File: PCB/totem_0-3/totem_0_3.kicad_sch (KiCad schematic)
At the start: 88 parts, among them J1 MJ-4PP-9, J2 MJ-4PP-9, U1 xiao-ble, U2 xiao-ble

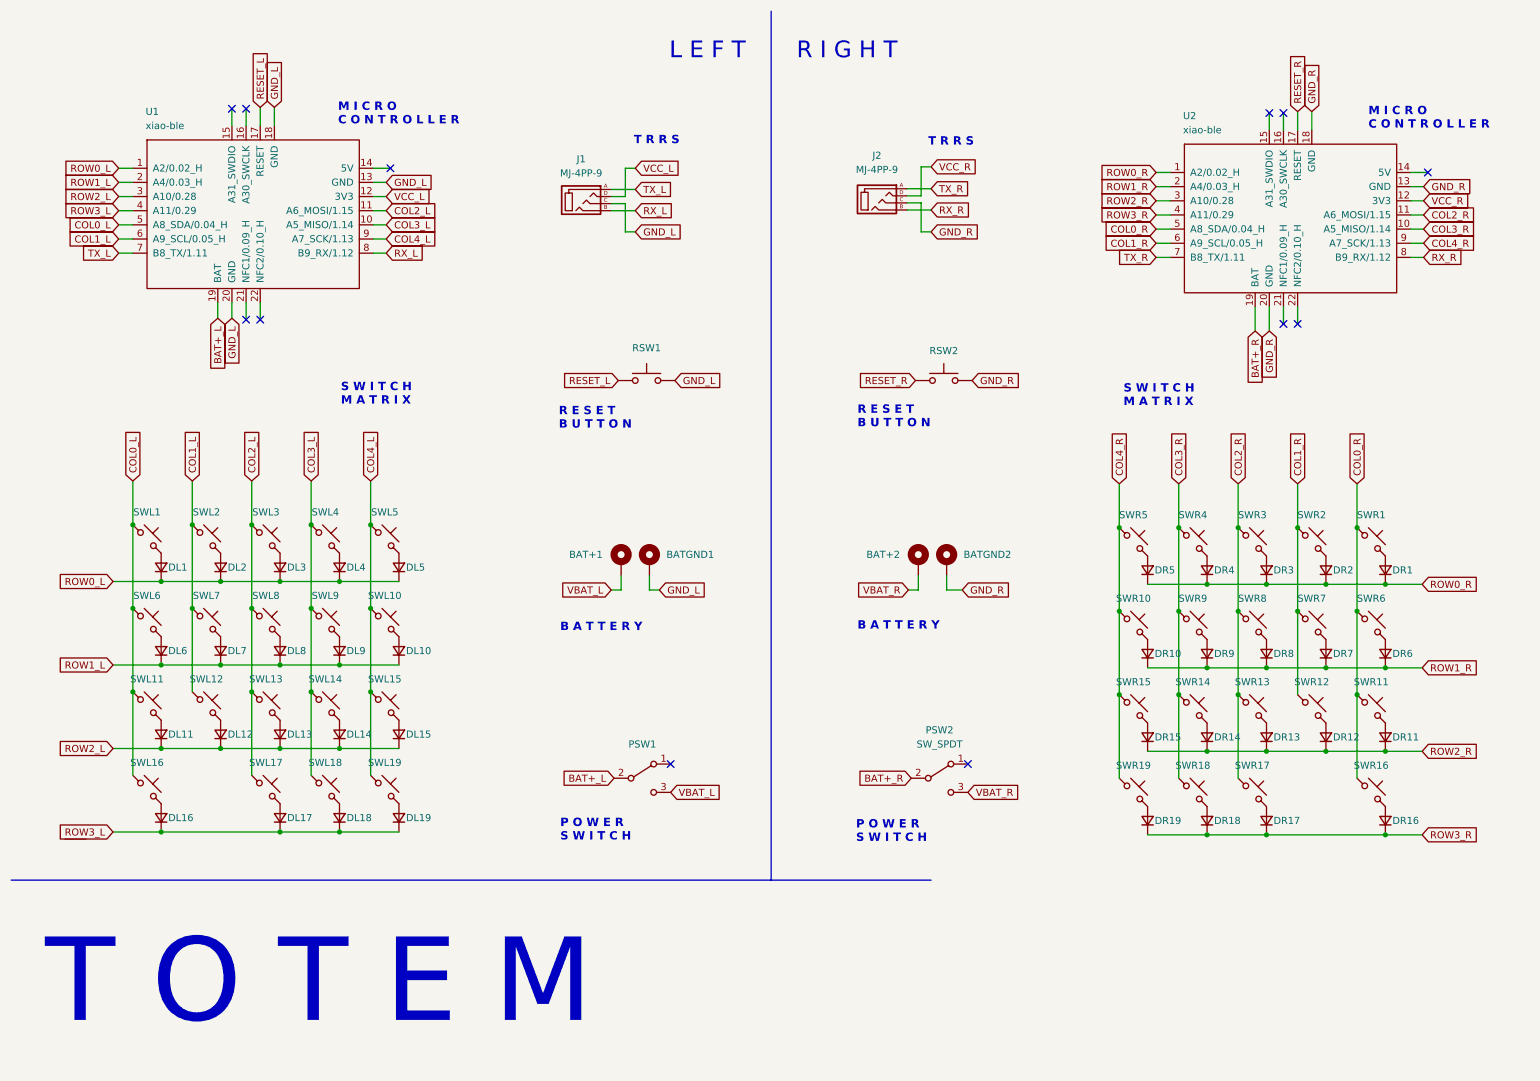
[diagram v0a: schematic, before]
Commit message: Convert to wired, before moving keys
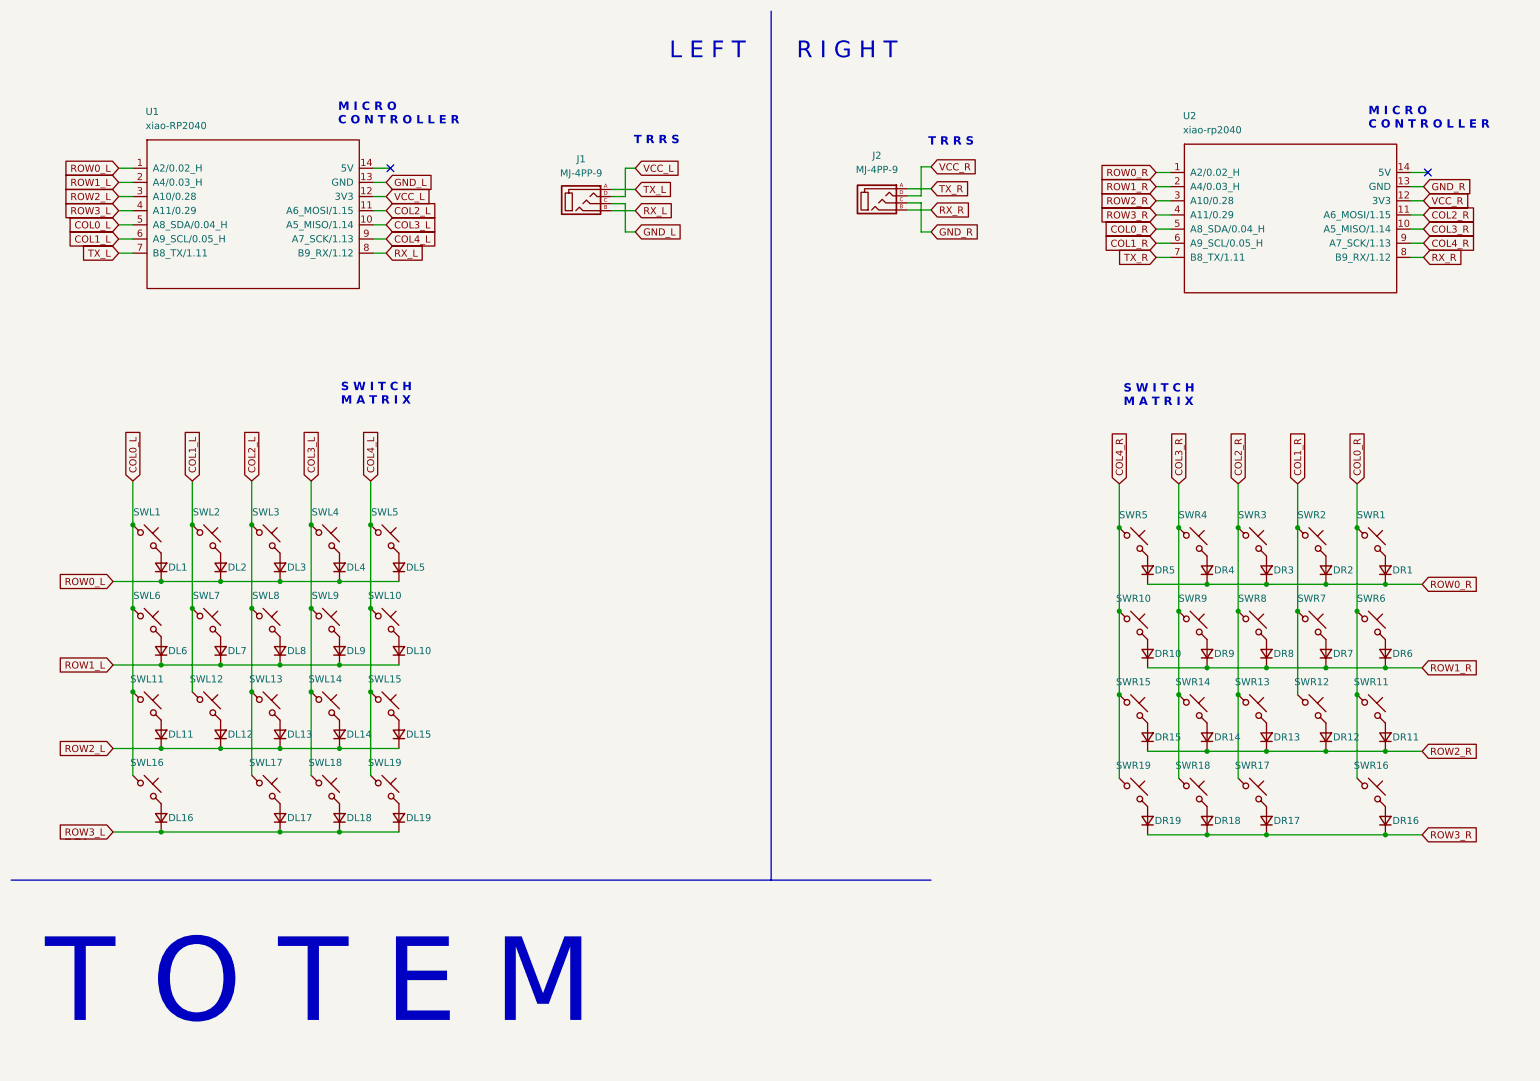
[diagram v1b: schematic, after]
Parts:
- removed BAT+1, BAT+2: +, TOTEMlib:BatteryPad, symbol Mechanical:MountingHole_Pad
- removed BATGND1, BATGND2: -, TOTEMlib:BatteryPad, symbol Mechanical:MountingHole_Pad
- removed PSW1, PSW2: SW_SPDT, TOTEMlib:MSK12C02, symbol Switch:SW_SPDT
- removed RSW1, RSW2: SW_Push, TOTEMlib:SKHLLCA010, symbol Switch:SW_Push
- U1: value xiao-ble -> xiao-RP2040; footprint TOTEMlib:xiao-ble-smd-cutout -> XIAO_PCB:xiao RP2040 MOUDLE14P-2.54-21X17.8MM; symbol mcu:xiao-ble -> xiaoRP2040:xiao-rp2040
- U2: value xiao-ble -> xiao-rp2040; footprint TOTEMlib:xiao-ble-smd-cutout -> XIAO_PCB:xiao RP2040 MOUDLE14P-2.54-21X17.8MM; symbol mcu:xiao-ble -> xiaoRP2040:xiao-rp2040
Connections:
- net GND_L: no longer U1.18 (GND), U1.20 (GND)
- net GND_R: no longer U2.18 (GND), U2.20 (GND)
- removed net BAT+_L: U1.19 (BAT)
- removed net BAT+_R: U2.19 (BAT)
- removed net RESET_L: U1.17 (RESET)
- removed net RESET_R: U2.17 (RESET)
- no-connect marks 12 -> 2
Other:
- note removed: "B A T T E R Y"
- note removed: "P O W E R S W I T C H"
- note removed: "R E S E T B U T T O N"
